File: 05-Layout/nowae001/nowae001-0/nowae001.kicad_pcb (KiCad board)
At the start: 2 copper layers, 25 x 16 mm, 28 parts, among them P1 USB_A_90, P2 CONN_4X1, Q1 IRLML6402, U1 FT230XQ, U2 TPS62152

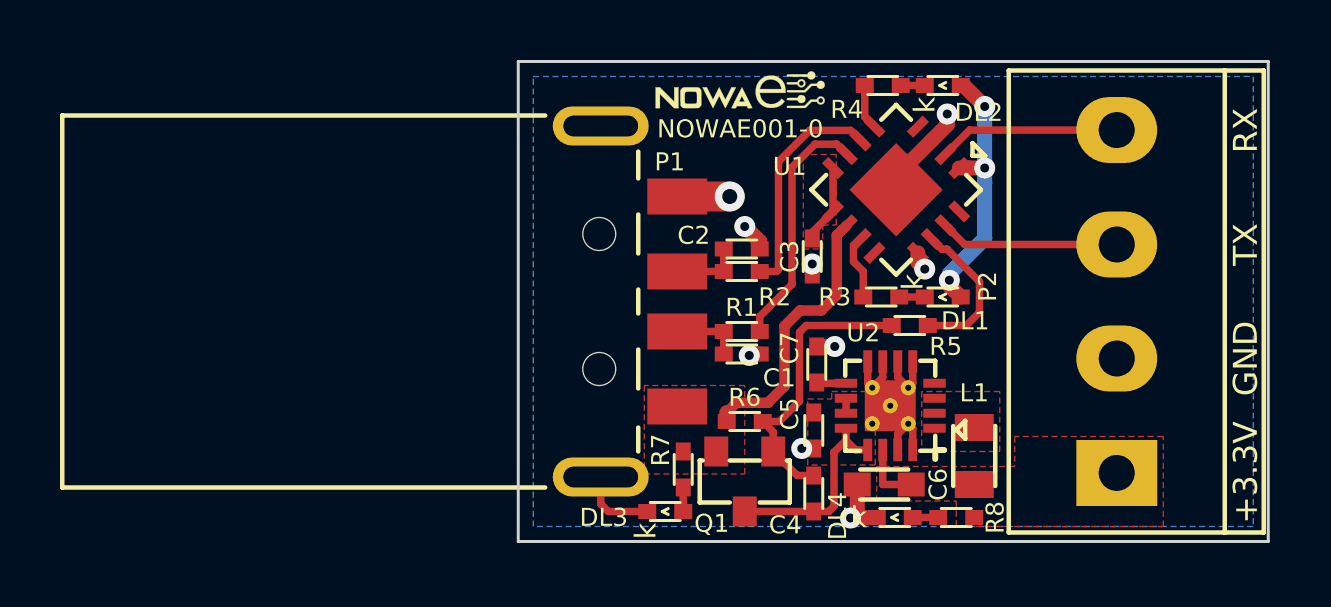
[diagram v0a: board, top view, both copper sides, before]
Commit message: Updated logos and license silkscreen
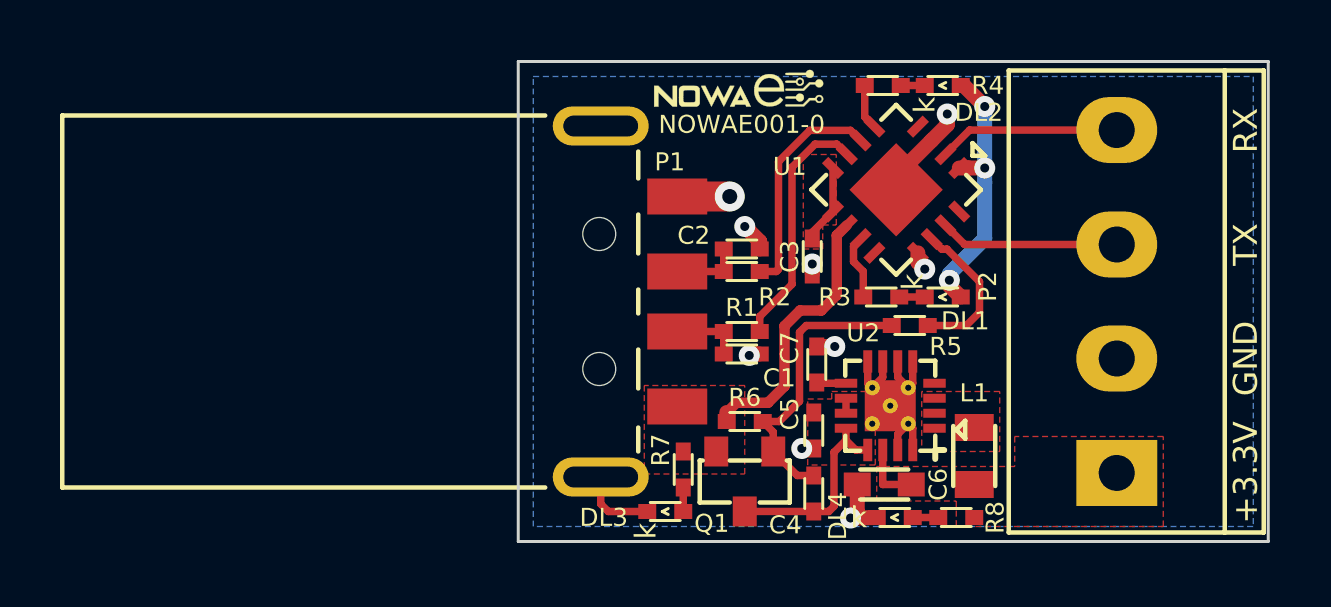
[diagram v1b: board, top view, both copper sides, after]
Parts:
- added G***: LOGO, LOGO:Untitled, F.Cu at (204.8, 128.3)
- G***: moved to B.Cu
- moved G*** 9.74 mm to (208.8, 139.6)
- moved G*** 7.23 mm to (208.9, 135.6)
- moved G*** 4.31 mm to (209.0, 129.5), turned to 180 degrees
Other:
- board text added: "WWW.NOWAE.IT"
